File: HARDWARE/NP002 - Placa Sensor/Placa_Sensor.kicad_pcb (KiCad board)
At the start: 2 copper layers, 28.5 x 55.4 mm, 25 parts, among them J1 Conn_01x05, J2 VGAS_Test, J3 GND_Test, J4 VDD_Test, J5 VREF_Test, J6 Conn_01x08, U1 LMP91000, U2 PIC16(L)F1829-I/SO, U3 CO gas sensor, U4 CO gas sensor

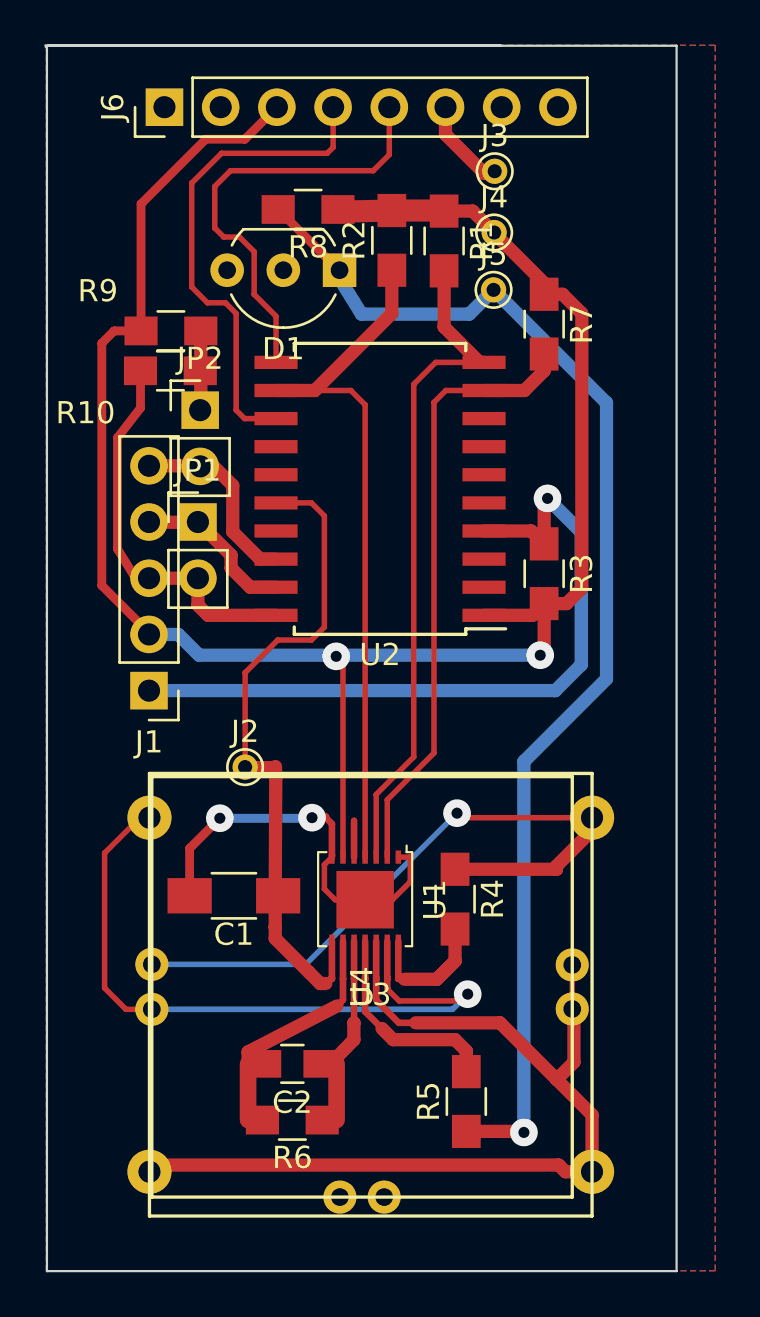
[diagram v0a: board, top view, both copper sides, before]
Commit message: 
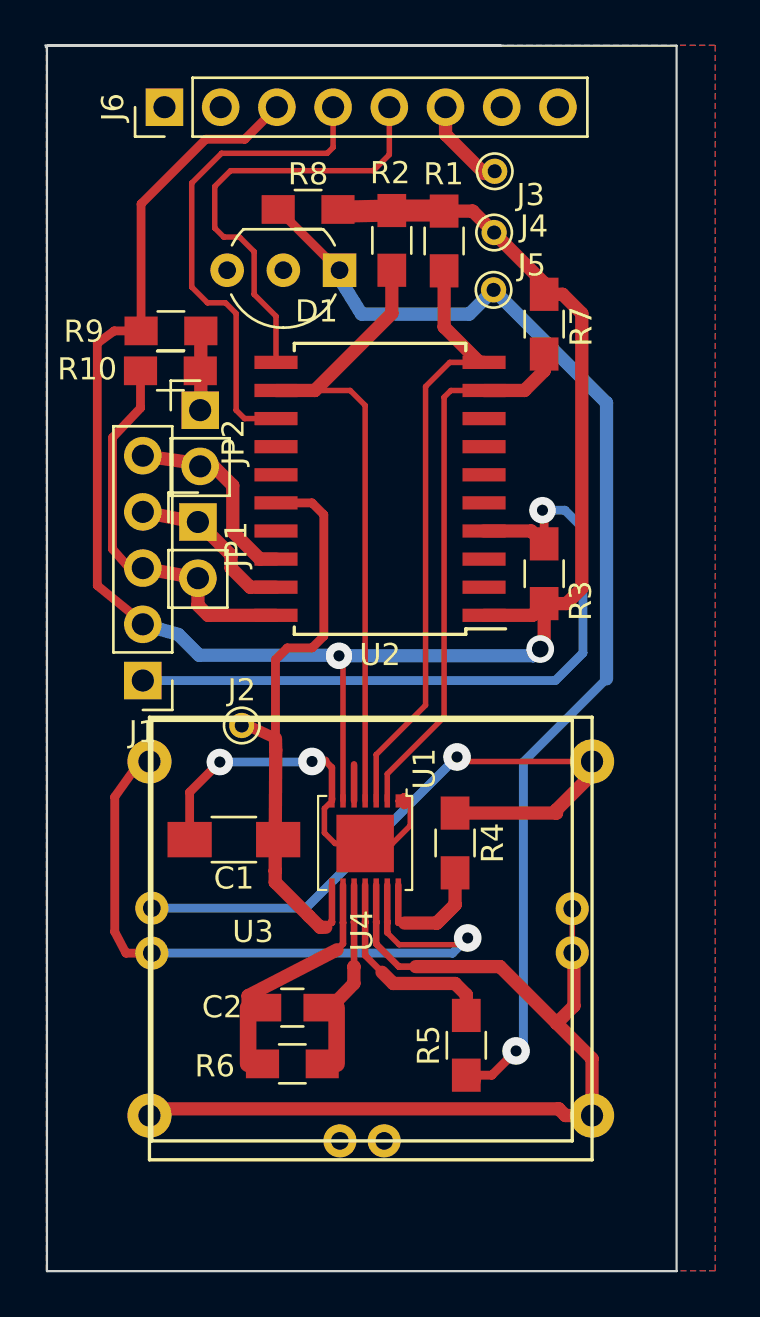
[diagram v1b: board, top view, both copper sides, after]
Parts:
- moved R5 2.54 mm to (259.1, 141.5)
- moved R6 2.54 mm to (251.2, 142.3)
- moved U4 2.54 mm to (254.4, 136.3)
- moved C1 2.54 mm to (248.6, 132.2)
- moved C2 2.54 mm to (251.2, 139.8)
- moved R4 2.54 mm to (258.6, 132.3)
- moved U1 2.54 mm to (254.5, 132.3)
- moved U3 2.54 mm to (254.7, 136.6)
- moved J2 1.89 mm to (248.9, 127.0)
- moved J1 0.54 mm to (244.4, 125.0)
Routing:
- net Vref: track 57.2 -> 53.7 mm
- net V_gas: track 30.6 -> 27.5 mm
- net SCL2: track 30.7 -> 27.7 mm
- net MENB: track 27.8 -> 25.1 mm
- net SDA2: track 31.6 -> 29.1 mm
- net VDD: track 91.0 -> 88.8 mm
- net GND: track 40.4 -> 42.0 mm
- net RE: track 32.3 -> 31.8 mm
- net Net-(J1-Pad1): track 33.2 -> 32.7 mm
